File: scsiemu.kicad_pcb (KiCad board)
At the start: 2 copper layers, 100 x 99 mm, 55 parts, among them J1 RasPi, J2 SCSI, J3 USB_POWER, J4 POWER 5V, J5 POWER 5V, J6 AT Power 5V (171826-4), J7 I2C Ext, J8 AT Power 5V (641737-1), U1 74LS641-1, U2 74LS641-1, U3 74LS641-1, U4 74LS641-1, U5 DS2105Z, U6 DS2105Z, U7 TL2218-285, U8 TL2218-285

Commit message: minor update
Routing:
- net GND: vias 184 -> 185
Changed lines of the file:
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@@
     (thickness 1.6)
     (drawings 95)
-    (tracks 1211)
+    (tracks 1212)
     (zones 0)
     (modules 55)
@@
       (layerselection 0x010fc_ffffffff)
       (usegerberextensions true)
-      (usegerberattributes false)
-      (usegerberadvancedattributes false)
+      (usegerberattributes true)
+      (usegerberadvancedattributes true)
       (creategerberjobfile false)
       (excludeedgelayer true)
@@
       (effects (font (size 1 1) (thickness 0.15)))
     )
+    (fp_circle (center 0 0) (end 3.5 0) (layer Cmts.User) (width 0.15))
+    (fp_circle (center 0 0) (end 3.75 0) (layer F.CrtYd) (width 0.05))
     (fp_text user %R (at 0.3 0) (layer F.Fab)
       (effects (font (size 1 1) (thickness 0.15)))
     )
-    (fp_circle (center 0 0) (end 3.5 0) (layer Cmts.User) (width 0.15))
-    (fp_circle (center 0 0) (end 3.75 0) (layer F.CrtYd) (width 0.05))
     (pad 1 np_thru_hole circle (at 0 0) (size 3.5 3.5) (drill 3.5) (layers *.Cu *.Mask)
       (net 125 "Net-(MH12-Pad1)"))
@@
       (effects (font (size 1 1) (thickness 0.15)))
     )
+    (fp_circle (center 0 0) (end 3.5 0) (layer Cmts.User) (width 0.15))
+    (fp_circle (center 0 0) (end 3.75 0) (layer F.CrtYd) (width 0.05))
     (fp_text user %R (at 0.3 0) (layer F.Fab)
       (effects (font (size 1 1) (thickness 0.15)))
     )
-    (fp_circle (center 0 0) (end 3.5 0) (layer Cmts.User) (width 0.15))
-    (fp_circle (center 0 0) (end 3.75 0) (layer F.CrtYd) (width 0.05))
     (pad 1 np_thru_hole circle (at 0 0) (size 3.5 3.5) (drill 3.5) (layers *.Cu *.Mask)
       (net 124 "Net-(MH11-Pad1)"))
@@
   (via (at 111.9632 105.9688) (size 0.7) (drill 0.3) (layers F.Cu B.Cu) (net 2))
   (via (at 111.9632 96.774) (size 0.7) (drill 0.3) (layers F.Cu B.Cu) (net 2))
+  (via (at 183.80964 50.24882) (size 0.8) (drill 0.3) (layers F.Cu B.Cu) (net 2))
   (segment (start 136.8298 49.277) (end 136.7536 49.3532) (width 0.6) (layer F.Cu) (net 3))
   (segment (start 136.8298 46.6233) (end 136.8298 49.277) (width 0.8) (layer F.Cu) (net 3))

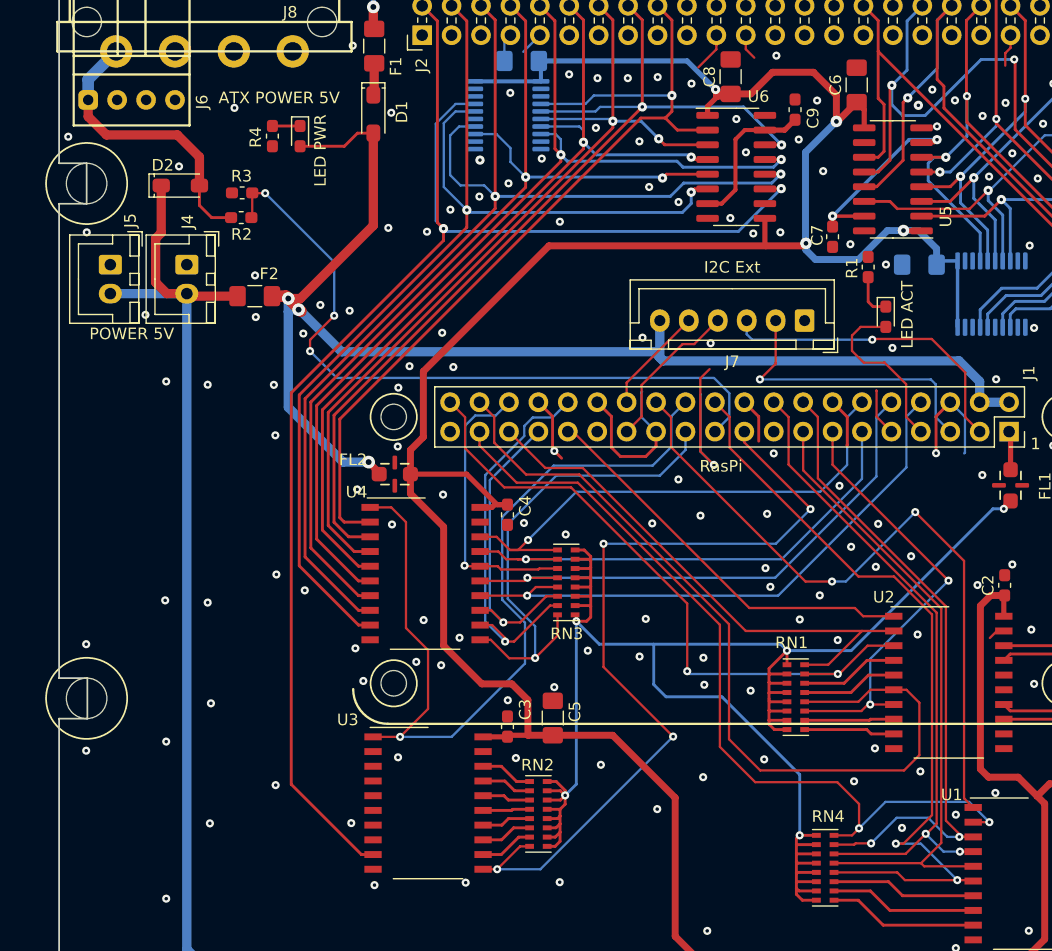
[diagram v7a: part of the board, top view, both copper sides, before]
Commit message: termination on/off jumper fix GND plane
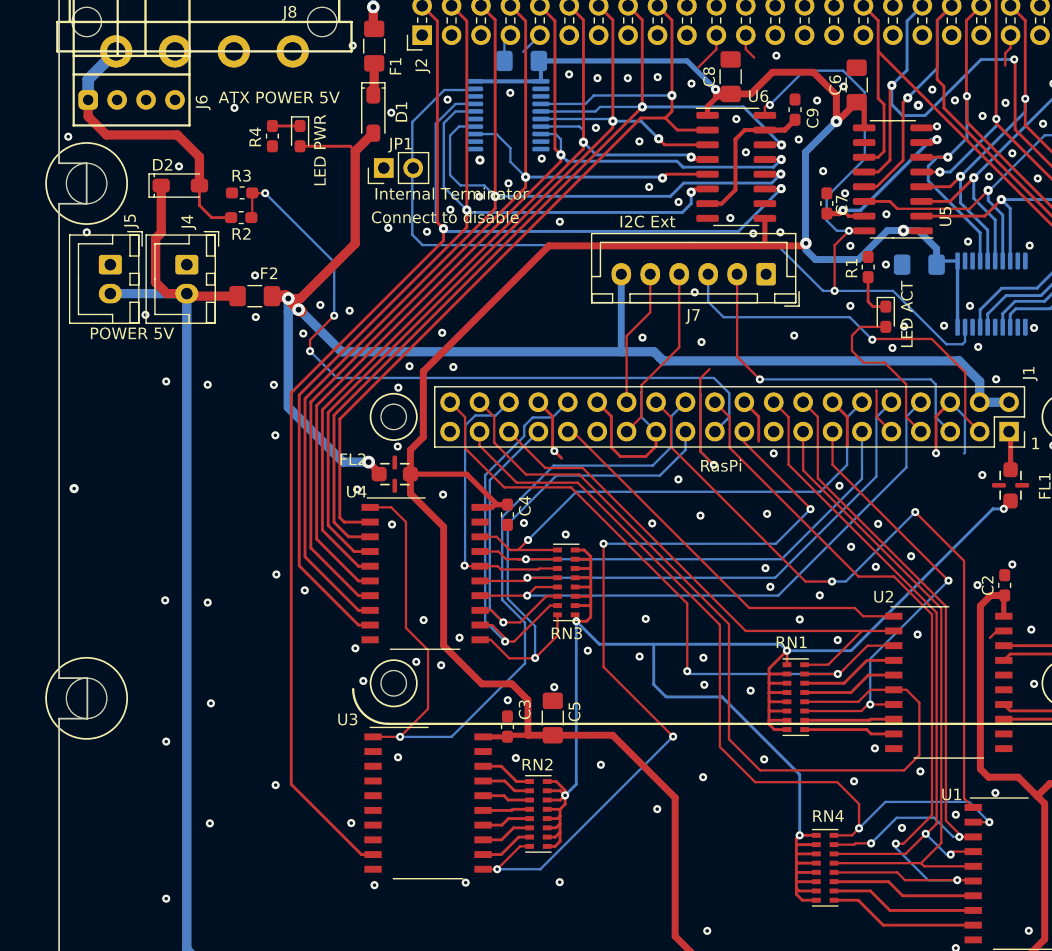
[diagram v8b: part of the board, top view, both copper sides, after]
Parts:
- added JP1: Internal Terminator, Connector_PinHeader_2.54mm:PinHeader_1x02_P2.54mm_Vertical, F.Cu at (137.7, 55.7)
- moved J7 5.20 mm to (170.7, 64.8)
- moved C7 2.91 mm to (175.9, 58.7), turned to 90 degrees
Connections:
- U5 pad 16: Net-(U5-Pad16) -> /INT_TERM
- U6 pad 16: Net-(U6-Pad16) -> /INT_TERM
- U7 pad 19: Net-(U7-Pad19) -> /INT_TERM
- U8 pad 19: Net-(U8-Pad19) -> /INT_TERM
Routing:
- net /INT_TERM: track 0.00 -> 102.5 mm, vias 0 -> 3
- net /I2C_SDA: track 27.1 -> 32.8 mm
- net /I2C_SCL: track 25.6 -> 29.9 mm
- net /EXT2: track 9.27 -> 11.9 mm
- net /EXT1: track 13.4 -> 15.5 mm
- net /5V_DC: track 118.7 -> 120.3 mm
- net Net-(C7-Pad1): track 16.8 -> 15.6 mm
- net GND: vias 185 -> 196
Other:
- board text added: "Connect to disable"
